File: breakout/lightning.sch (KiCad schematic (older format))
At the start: 14 parts, among them J1 CONN_01X02, J2 CONN_01X03, J3 CONN_01X07, U1 AS3935

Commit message: [add] Matching footprints to components
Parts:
- C1, C2, C3, C4, C5, C6: footprint (none) -> Capacitors_SMD:C_1206_HandSoldering
- J1: footprint (none) -> Pin_Headers:Pin_Header_Straight_1x02_Pitch1.27mm
- J2: footprint (none) -> Pin_Headers:Pin_Header_Straight_1x03_Pitch2.54mm
- J3: footprint (none) -> Pin_Headers:Pin_Header_Straight_1x07_Pitch1.27mm
- L1: footprint (none) -> MA5532-AE:MA5532-AE
- R1, R2, R3: footprint (none) -> Resistors_SMD:R_1206_HandSoldering
- U1: footprint (none) -> Housings_DFN_QFN:QFN-16-1EP_4x4mm_Pitch0.65mm
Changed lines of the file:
@@
 LIBS:contrib
 LIBS:valves
+LIBS:lightning-cache
 EELAYER 25 0
 EELAYER END
@@
 F 0 "U1" H 5900 3600 60  0000 C CNN
 F 1 "AS3935" H 5900 4100 60  0000 C CNN
-F 2 "" H 5900 3850 60  0001 C CNN
+F 2 "Housings_DFN_QFN:QFN-16-1EP_4x4mm_Pitch0.65mm" H 5900 3850 60  0001 C CNN
 F 3 "" H 5900 3850 60  0001 C CNN
 	1    5900 3850
@@
 F 0 "C3" H 5210 3570 50  0000 L CNN
 F 1 "10uF" H 5210 3420 50  0000 L CNN
-F 2 "" H 5200 3500 50  0001 C CNN
+F 2 "Capacitors_SMD:C_1206_HandSoldering" H 5200 3500 50  0001 C CNN
 F 3 "" H 5200 3500 50  0001 C CNN
 	1    5200 3500
@@
 F 0 "R1" H 4830 3870 50  0000 L CNN
 F 1 "10k" H 4830 3810 50  0000 L CNN
-F 2 "" H 4800 3850 50  0001 C CNN
+F 2 "Resistors_SMD:R_1206_HandSoldering" H 4800 3850 50  0001 C CNN
 F 3 "" H 4800 3850 50  0001 C CNN
 	1    4800 3850
@@
 F 0 "C1" H 4110 3920 50  0000 L CNN
 F 1 "270pF" H 4150 3800 50  0000 L CNN
-F 2 "" H 4100 3850 50  0001 C CNN
+F 2 "Capacitors_SMD:C_1206_HandSoldering" H 4100 3850 50  0001 C CNN
 F 3 "" H 4100 3850 50  0001 C CNN
 	1    4100 3850
@@
 F 0 "C2" H 4460 3920 50  0000 L CNN
 F 1 "680pF" H 4500 3800 50  0000 L CNN
-F 2 "" H 4450 3850 50  0001 C CNN
+F 2 "Capacitors_SMD:C_1206_HandSoldering" H 4450 3850 50  0001 C CNN
 F 3 "" H 4450 3850 50  0001 C CNN
 	1    4450 3850
@@
 F 0 "L1" V 3500 3850 50  0000 C CNN
 F 1 "MA5532-AE" H 3800 3850 50  0000 C CNN
-F 2 "" H 3550 3850 50  0001 C CNN
+F 2 "MA5532-AE:MA5532-AE" H 3550 3850 50  0001 C CNN
 F 3 "" H 3550 3850 50  0001 C CNN
 	1    3550 3850
@@
 F 0 "J1" H 3350 2450 50  0000 C CNN
 F 1 "CONN_01X02" V 3450 2300 50  0000 C CNN
-F 2 "" H 3350 2300 50  0001 C CNN
+F 2 "Pin_Headers:Pin_Header_Straight_1x02_Pitch1.27mm" H 3350 2300 50  0001 C CNN
 F 3 "" H 3350 2300 50  0001 C CNN
 	1    3350 2300
@@
 F 0 "J2" H 4200 2500 50  0000 C CNN
 F 1 "CONN_01X03" V 4300 2300 50  0000 C CNN
-F 2 "" H 4200 2300 50  0001 C CNN
+F 2 "Pin_Headers:Pin_Header_Straight_1x03_Pitch2.54mm" H 4200 2300 50  0001 C CNN
 F 3 "" H 4200 2300 50  0001 C CNN
 	1    4200 2300
@@
 F 0 "C5" H 5860 5120 50  0000 L CNN
 F 1 "1uF" H 5860 4970 50  0000 L CNN
-F 2 "" H 5850 5050 50  0001 C CNN
+F 2 "Capacitors_SMD:C_1206_HandSoldering" H 5850 5050 50  0001 C CNN
 F 3 "" H 5850 5050 50  0001 C CNN
 	1    5850 5050
@@
 F 0 "J3" H 8250 4050 50  0000 C CNN
 F 1 "CONN_01X07" V 8350 3650 50  0000 C CNN
-F 2 "" H 8250 3650 50  0001 C CNN
+F 2 "Pin_Headers:Pin_Header_Straight_1x07_Pitch1.27mm" H 8250 3650 50  0001 C CNN
 F 3 "" H 8250 3650 50  0001 C CNN
 	1    8250 3650
@@
 F 0 "R3" H 7030 3620 50  0000 L CNN
 F 1 "10k" H 7030 3560 50  0000 L CNN
-F 2 "" H 7000 3600 50  0001 C CNN
+F 2 "Resistors_SMD:R_1206_HandSoldering" H 7000 3600 50  0001 C CNN
 F 3 "" H 7000 3600 50  0001 C CNN
 	1    7000 3600
@@
 F 0 "R2" H 6330 2820 50  0000 L CNN
 F 1 "10k" H 6330 2760 50  0000 L CNN
-F 2 "" H 6300 2800 50  0001 C CNN
+F 2 "Resistors_SMD:R_1206_HandSoldering" H 6300 2800 50  0001 C CNN
 F 3 "" H 6300 2800 50  0001 C CNN
 	1    6300 2800
@@
 F 0 "C4" H 5510 5070 50  0000 L CNN
 F 1 "100nF" H 5510 4920 50  0000 L CNN
-F 2 "" H 5500 5000 50  0001 C CNN
+F 2 "Capacitors_SMD:C_1206_HandSoldering" H 5500 5000 50  0001 C CNN
 F 3 "" H 5500 5000 50  0001 C CNN
 	1    5500 5000
@@
 F 0 "C6" H 6310 5070 50  0000 L CNN
 F 1 "1uF" H 6310 4920 50  0000 L CNN
-F 2 "" H 6300 5000 50  0001 C CNN
+F 2 "Capacitors_SMD:C_1206_HandSoldering" H 6300 5000 50  0001 C CNN
 F 3 "" H 6300 5000 50  0001 C CNN
 	1    6300 5000

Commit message: [fix] Wrong size pitch for the connectors.
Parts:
- J1: footprint Pin_Headers:Pin_Header_Straight_1x02_Pitch1.27mm -> Pin_Headers:Pin_Header_Straight_1x02_Pitch2.54mm
- J3: footprint Pin_Headers:Pin_Header_Straight_1x07_Pitch1.27mm -> Pin_Headers:Pin_Header_Straight_1x07_Pitch2.54mm
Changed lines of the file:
@@
 F 0 "J1" H 3350 2450 50  0000 C CNN
 F 1 "CONN_01X02" V 3450 2300 50  0000 C CNN
-F 2 "Pin_Headers:Pin_Header_Straight_1x02_Pitch1.27mm" H 3350 2300 50  0001 C CNN
+F 2 "Pin_Headers:Pin_Header_Straight_1x02_Pitch2.54mm" H 3350 2300 50  0001 C CNN
 F 3 "" H 3350 2300 50  0001 C CNN
 	1    3350 2300
@@
 F 0 "J3" H 8250 4050 50  0000 C CNN
 F 1 "CONN_01X07" V 8350 3650 50  0000 C CNN
-F 2 "Pin_Headers:Pin_Header_Straight_1x07_Pitch1.27mm" H 8250 3650 50  0001 C CNN
+F 2 "Pin_Headers:Pin_Header_Straight_1x07_Pitch2.54mm" H 8250 3650 50  0001 C CNN
 F 3 "" H 8250 3650 50  0001 C CNN
 	1    8250 3650

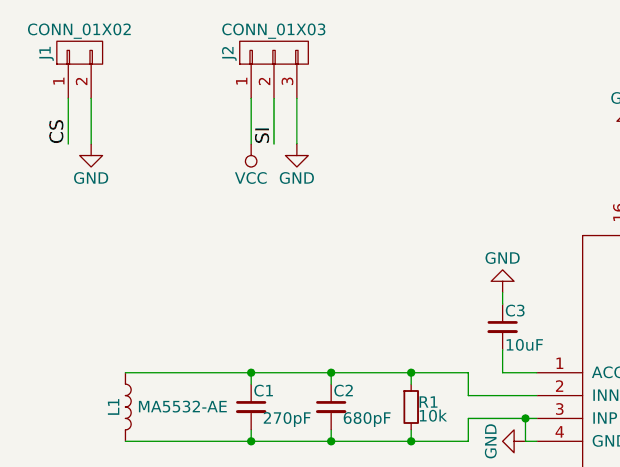
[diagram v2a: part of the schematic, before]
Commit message: [enh] Use solder jumper instead of physical one.
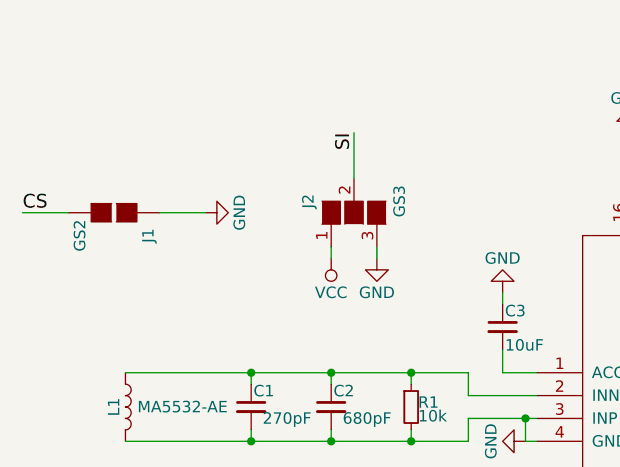
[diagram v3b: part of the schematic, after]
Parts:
- removed J1: CONN_01X02, Pin_Headers:Pin_Header_Straight_1x02_Pitch2.54mm, symbol CONN_01X02
- removed J2: CONN_01X03, Pin_Headers:Pin_Header_Straight_1x03_Pitch2.54mm, symbol CONN_01X03
- added J1: GS2, Connectors:GS2, symbol GS2
- added J2: GS3, Connectors:GS3, symbol GS3
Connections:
- net CS: now also J1.2 (G2)
- net GND: now also J1.1 (G1), J2.3 (G3)
- net SI: now also J2.2 (G2)
- net VCC: now also J2.1 (G1)
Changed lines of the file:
@@
 Connection ~ 4100 3700
 Connection ~ 4100 4000
-$Comp
-L CONN_01X02 J1
-U 1 1 59960474
-P 3350 2300
-F 0 "J1" H 3350 2450 50  0000 C CNN
-F 1 "CONN_01X02" V 3450 2300 50  0000 C CNN
-F 2 "Pin_Headers:Pin_Header_Straight_1x02_Pitch2.54mm" H 3350 2300 50  0001 C CNN
-F 3 "" H 3350 2300 50  0001 C CNN
-	1    3350 2300
-	0    -1   -1   0
-$EndComp
-$Comp
-L CONN_01X03 J2
-U 1 1 599605D8
-P 4200 2300
-F 0 "J2" H 4200 2500 50  0000 C CNN
-F 1 "CONN_01X03" V 4300 2300 50  0000 C CNN
-F 2 "Pin_Headers:Pin_Header_Straight_1x03_Pitch2.54mm" H 4200 2300 50  0001 C CNN
-F 3 "" H 4200 2300 50  0001 C CNN
-	1    4200 2300
-	0    -1   -1   0
-$EndComp
-Wire Wire Line
-	3300 2500 3300 2700
-Wire Wire Line
-	3400 2500 3400 2700
-Text Label 3300 2700 1    60   ~ 0
-CS
-Wire Wire Line
-	4100 2500 4100 2700
-Wire Wire Line
-	4200 2500 4200 2700
-Wire Wire Line
-	4300 2500 4300 2700
-Text Label 4200 2700 1    60   ~ 0
+Text Label 4550 2650 3    60   ~ 0
 SI
 Wire Wire Line
@@
 $Comp
 L GND #PWR03
-U 1 1 599608A1
-P 3400 2700
-F 0 "#PWR03" H 3400 2450 50  0001 C CNN
-F 1 "GND" H 3400 2550 50  0000 C CNN
-F 2 "" H 3400 2700 50  0001 C CNN
-F 3 "" H 3400 2700 50  0001 C CNN
-	1    3400 2700
-	1    0    0    -1
-$EndComp
-$Comp
-L GND #PWR04
 U 1 1 599608CD
-P 4300 2700
-F 0 "#PWR04" H 4300 2450 50  0001 C CNN
-F 1 "GND" H 4300 2550 50  0000 C CNN
-F 2 "" H 4300 2700 50  0001 C CNN
-F 3 "" H 4300 2700 50  0001 C CNN
-	1    4300 2700
-	1    0    0    -1
-$EndComp
-$Comp
-L VCC #PWR05
+P 4650 3200
+F 0 "#PWR03" H 4650 2950 50  0001 C CNN
+F 1 "GND" H 4650 3050 50  0000 C CNN
+F 2 "" H 4650 3200 50  0001 C CNN
+F 3 "" H 4650 3200 50  0001 C CNN
+	1    4650 3200
+	1    0    0    -1
+$EndComp
+$Comp
+L VCC #PWR04
 U 1 1 599608F9
-P 4100 2700
-F 0 "#PWR05" H 4100 2550 50  0001 C CNN
-F 1 "VCC" H 4100 2850 50  0000 C CNN
-F 2 "" H 4100 2700 50  0001 C CNN
-F 3 "" H 4100 2700 50  0001 C CNN
-	1    4100 2700
+P 4450 3200
+F 0 "#PWR04" H 4450 3050 50  0001 C CNN
+F 1 "VCC" H 4450 3350 50  0000 C CNN
+F 2 "" H 4450 3200 50  0001 C CNN
+F 3 "" H 4450 3200 50  0001 C CNN
+	1    4450 3200
 	-1   0    0    1
 $EndComp
@@
 Connection ~ 5750 2800
 $Comp
-L GND #PWR06
+L GND #PWR05
 U 1 1 59960A70
 P 5750 2650
-F 0 "#PWR06" H 5750 2400 50  0001 C CNN
+F 0 "#PWR05" H 5750 2400 50  0001 C CNN
 F 1 "GND" H 5750 2500 50  0000 C CNN
 F 2 "" H 5750 2650 50  0001 C CNN
@@
 	5850 5150 5850 5200
 $Comp
-L GND #PWR07
+L GND #PWR06
 U 1 1 59960C8C
 P 5850 5200
-F 0 "#PWR07" H 5850 4950 50  0001 C CNN
+F 0 "#PWR06" H 5850 4950 50  0001 C CNN
 F 1 "GND" H 5850 5050 50  0000 C CNN
 F 2 "" H 5850 5200 50  0001 C CNN
@@
 Connection ~ 5850 5450
 $Comp
-L VCC #PWR08
+L VCC #PWR07
 U 1 1 59960D1D
 P 5850 5550
-F 0 "#PWR08" H 5850 5400 50  0001 C CNN
+F 0 "#PWR07" H 5850 5400 50  0001 C CNN
 F 1 "VCC" H 5850 5700 50  0000 C CNN
 F 2 "" H 5850 5550 50  0001 C CNN
@@
 	8050 3350 7600 3350
 $Comp
-L VCC #PWR09
+L VCC #PWR08
 U 1 1 59961001
 P 7600 3350
-F 0 "#PWR09" H 7600 3200 50  0001 C CNN
+F 0 "#PWR08" H 7600 3200 50  0001 C CNN
 F 1 "VCC" H 7600 3500 50  0000 C CNN
 F 2 "" H 7600 3350 50  0001 C CNN
@@
 	7600 3450 8050 3450
 $Comp
-L GND #PWR010
+L GND #PWR09
 U 1 1 59961061
 P 7600 3450
-F 0 "#PWR010" H 7600 3200 50  0001 C CNN
+F 0 "#PWR09" H 7600 3200 50  0001 C CNN
 F 1 "GND" H 7600 3300 50  0000 C CNN
 F 2 "" H 7600 3450 50  0001 C CNN
@@
 	7000 3500 7000 3400
 $Comp
-L VCC #PWR011
+L VCC #PWR010
 U 1 1 599617F9
 P 7000 3400
-F 0 "#PWR011" H 7000 3250 50  0001 C CNN
+F 0 "#PWR010" H 7000 3250 50  0001 C CNN
 F 1 "VCC" H 7000 3550 50  0000 C CNN
 F 2 "" H 7000 3400 50  0001 C CNN
@@
 	6400 2800 6550 2800
 $Comp
-L VCC #PWR012
+L VCC #PWR011
 U 1 1 599619AD
 P 6550 2800
-F 0 "#PWR012" H 6550 2650 50  0001 C CNN
+F 0 "#PWR011" H 6550 2650 50  0001 C CNN
 F 1 "VCC" H 6550 2950 50  0000 C CNN
 F 2 "" H 6550 2800 50  0001 C CNN
@@
 	5400 5000 5200 5000
 $Comp
-L GND #PWR013
+L GND #PWR012
 U 1 1 59961BC0
 P 5200 5000
-F 0 "#PWR013" H 5200 4750 50  0001 C CNN
+F 0 "#PWR012" H 5200 4750 50  0001 C CNN
 F 1 "GND" H 5200 4850 50  0000 C CNN
 F 2 "" H 5200 5000 50  0001 C CNN
@@
 	6400 5000 6650 5000
 $Comp
-L GND #PWR014
+L GND #PWR013
 U 1 1 59961CD1
 P 6650 5000
-F 0 "#PWR014" H 6650 4750 50  0001 C CNN
+F 0 "#PWR013" H 6650 4750 50  0001 C CNN
 F 1 "GND" H 6650 4850 50  0000 C CNN
 F 2 "" H 6650 5000 50  0001 C CNN
@@
 	0    -1   -1   0
 $EndComp
+$Comp
+L GS3 J2
+U 1 1 59BD4EA1
+P 4550 3000
+F 0 "J2" H 4600 3200 50  0000 C CNN
+F 1 "GS3" H 4600 2801 50  0000 C CNN
+F 2 "Connectors:GS3" V 4638 2926 50  0001 C CNN
+F 3 "" H 4550 3000 50  0001 C CNN
+	1    4550 3000
+	0    -1   -1   0
+$EndComp
+$Comp
+L GS2 J1
+U 1 1 59BD4F62
+P 3500 3000
+F 0 "J1" H 3600 3150 50  0000 C CNN
+F 1 "GS2" H 3600 2851 50  0000 C CNN
+F 2 "Connectors:GS2" V 3574 3000 50  0001 C CNN
+F 3 "" H 3500 3000 50  0001 C CNN
+	1    3500 3000
+	0    1    1    0
+$EndComp
+Wire Wire Line
+	3300 3000 3100 3000
+Text Label 3100 3000 0    60   ~ 0
+CS
+$Comp
+L GND #PWR014
+U 1 1 59BD51A6
+P 3900 3000
+F 0 "#PWR014" H 3900 2750 50  0001 C CNN
+F 1 "GND" H 3900 2850 50  0000 C CNN
+F 2 "" H 3900 3000 50  0001 C CNN
+F 3 "" H 3900 3000 50  0001 C CNN
+	1    3900 3000
+	0    -1   -1   0
+$EndComp
+Wire Wire Line
+	3900 3000 3700 3000
+Wire Wire Line
+	4550 2850 4550 2650
+Wire Wire Line
+	4450 3150 4450 3200
+Wire Wire Line
+	4650 3150 4650 3200
 $EndSCHEMATC
